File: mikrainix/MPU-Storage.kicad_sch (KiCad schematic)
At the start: 6 parts, among them J4 MicroSD, U7 RV1106G3

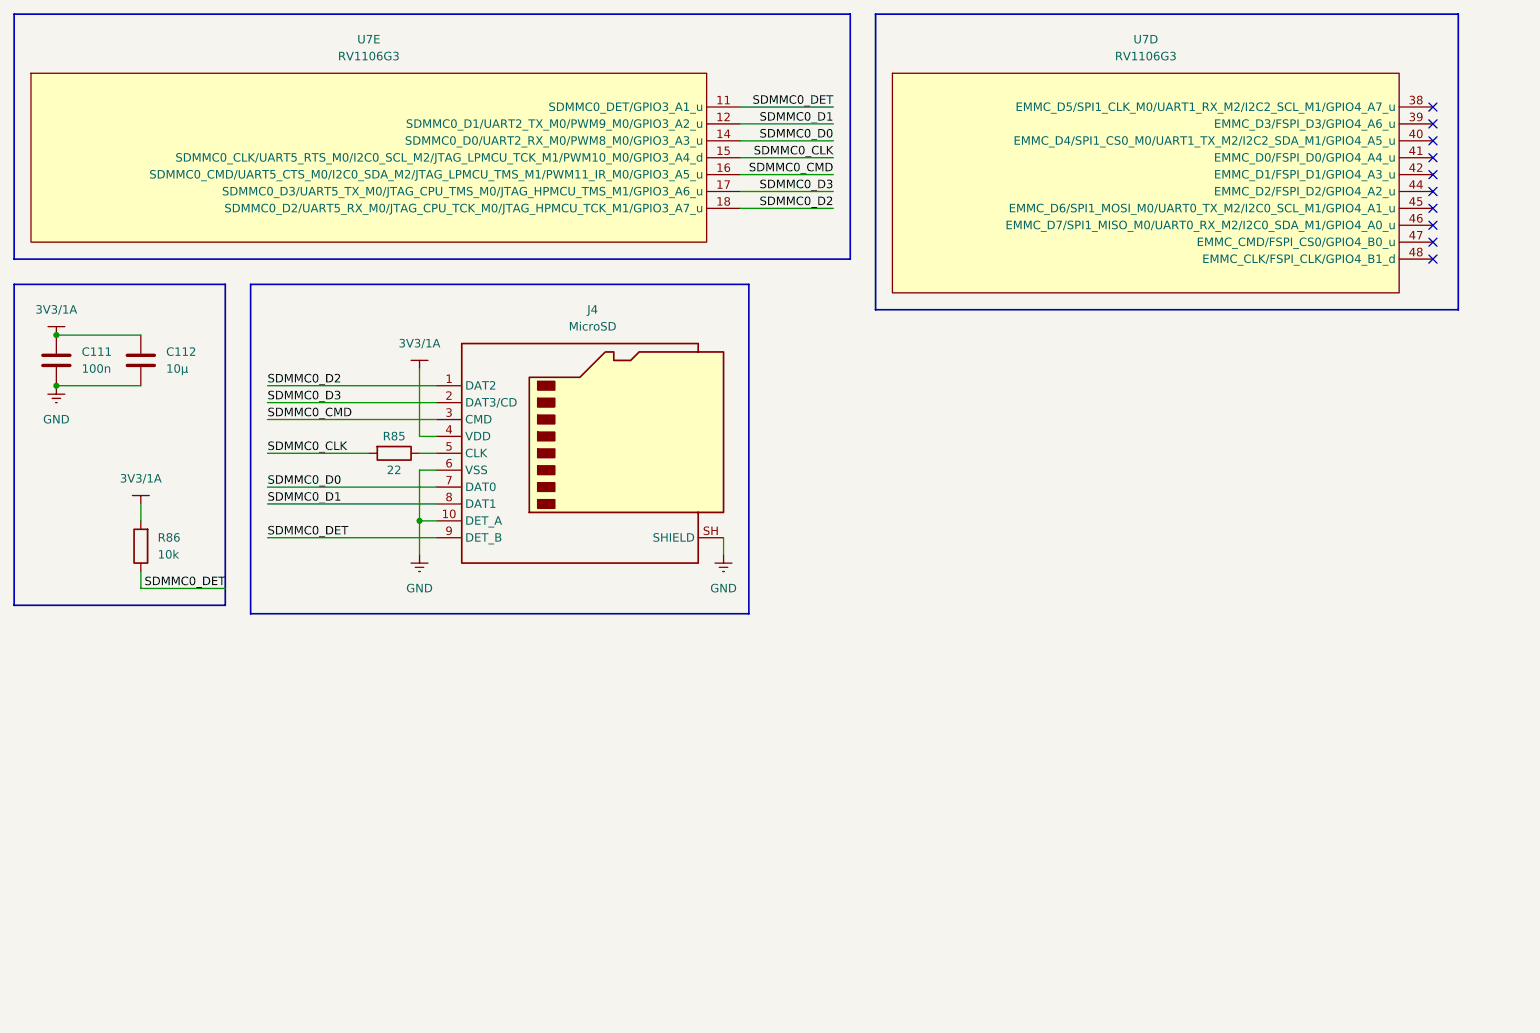
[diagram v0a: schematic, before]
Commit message: add ESD protection
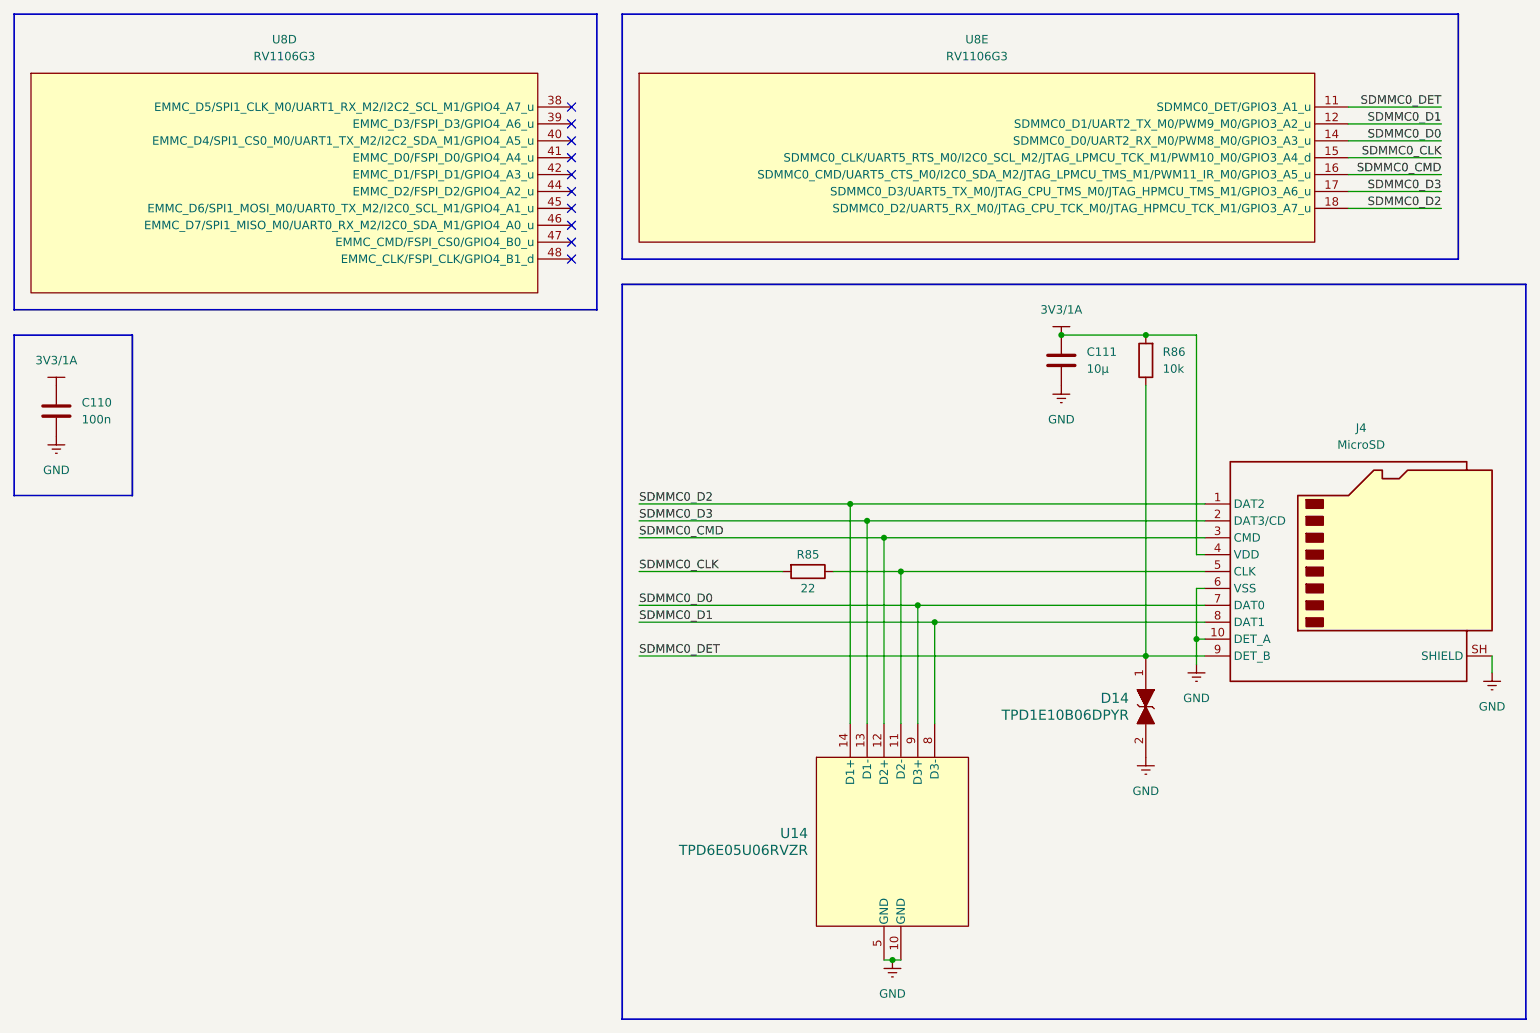
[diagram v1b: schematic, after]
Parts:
- removed C112: 10µ, symbol Device:C
- removed U7: RV1106G3, mikrainix-RV1106G3:QFN35P1230X1230X90-129N, symbol mikrainix-RV1106G3:RV1106G3
- added C110: 100n, symbol Device:C
- added D14: TPD1E10B06DPYR, mikrainix-TPD1E10B06DPYR:DIO_TPD1E10B06DPYR, symbol mikrainix-ESD_SYM:ESDx1
- added U14: TPD6E05U06RVZR, mikrainix-TPD6E05U06RVZR:RVZ0014A, symbol mikrainix-TPD6E05U06RVZR:TPD6E05U06RVZR
- added U8: RV1106G3, mikrainix-RV1106G3:QFN35P1230X1230X90-129N, symbol mikrainix-RV1106G3:RV1106G3
- C111: value 100n -> 10µ
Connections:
- net 3V3/1A: now also C110.1
- net GND: now also C110.2, D14.2, U14.10 (GND), U14.5 (GND)
- net SDMMC0_CLK: now also U8.15 (SDMMC0_CLK/UART5_RTS_M0/I2C0_SCL_M2/JTAG_LPMCU_TCK_M1/PWM10_M0/GPIO3_A4_d)
- net SDMMC0_CMD: now also U14.12 (D2+), U8.16 (SDMMC0_CMD/UART5_CTS_M0/I2C0_SDA_M2/JTAG_LPMCU_TMS_M1/PWM11_IR_M0/GPIO3_A5_u)
- net SDMMC0_D0: now also U14.9 (D3+), U8.14 (SDMMC0_D0/UART2_RX_M0/PWM8_M0/GPIO3_A3_u)
- net SDMMC0_D1: now also U14.8 (D3-), U8.12 (SDMMC0_D1/UART2_TX_M0/PWM9_M0/GPIO3_A2_u)
- net SDMMC0_D2: now also U14.14 (D1+), U8.18 (SDMMC0_D2/UART5_RX_M0/JTAG_CPU_TCK_M0/JTAG_HPMCU_TCK_M1/GPIO3_A7_u)
- net SDMMC0_D3: now also U14.13 (D1-), U8.17 (SDMMC0_D3/UART5_TX_M0/JTAG_CPU_TMS_M0/JTAG_HPMCU_TMS_M1/GPIO3_A6_u)
- net SDMMC0_DET: now also D14.1, U8.11 (SDMMC0_DET/GPIO3_A1_u)
- net at J4.5 (CLK), R85.1: now also U14.11 (D2-)
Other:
- moved on the sheet: J4, R85
